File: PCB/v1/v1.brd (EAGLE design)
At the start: 53 x 39 mm, 62 parts, among them U2 AT24C512C-SHD-B

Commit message: quickly added antenna
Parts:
- added U$7: ANTENNA_1LEFT, ant-planar-1:SWRA117D_LEFT
- moved C7 1.68 mm to (32.4, 27.3), turned to 90 degrees
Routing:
- net N$39: track 48.5 -> 40.3 mm
- net N$74: track 0.00 -> 7.95 mm
- net N$43: track 1.63 -> 3.58 mm
- net GND: track 184.4 -> 182.6 mm
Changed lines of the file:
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@@
 <setting verticaltext="up"/>
 </settings>
-<grid distance="0.25" unitdist="mm" unit="mm" style="lines" multiple="1" display="no" altdistance="0.125" altunitdist="mm" altunit="mm"/>
+<grid distance="0.25" unitdist="mm" unit="mm" style="lines" multiple="1" display="no" altdistance="0.01" altunitdist="mm" altunit="mm"/>
 <layers>
 <layer number="1" name="Top" color="4" fill="1" visible="yes" active="yes"/>
@@
 <attribute name="OC_FARNELL" value="-" x="-13.49825" y="-11.42925" size="1.778" layer="27" rot="R270" display="off"/>
 </element>
-<element name="C7" library="AVX_By_element14_Batch_1" package="CAPC1005X60N" value="0.5pF" x="31.27895" y="26.062">
-<attribute name="OC_NEWARK" value="32T8767" x="103.66895" y="-18.388" size="1.778" layer="27" display="off"/>
-<attribute name="TOLERANCE" value="±.1 pF" x="103.66895" y="-18.388" size="1.778" layer="27" display="off"/>
-<attribute name="MPN" value="UQCL2A0R5BAT2A/500" x="103.66895" y="-18.388" size="1.778" layer="27" display="off"/>
-<attribute name="SUPPLIER" value="AVX" x="103.66895" y="-18.388" size="1.778" layer="27" display="off"/>
-<attribute name="VOLTAGERATING" value="200V" x="103.66895" y="-18.388" size="1.778" layer="27" display="off"/>
-<attribute name="OC_FARNELL" value="-" x="103.66895" y="-18.388" size="1.778" layer="27" display="off"/>
+<element name="C7" library="AVX_By_element14_Batch_1" package="CAPC1005X60N" value="0.5pF" x="32.438" y="27.27895" rot="R90">
+<attribute name="OC_NEWARK" value="32T8767" x="76.888" y="99.66895" size="1.778" layer="27" rot="R90" display="off"/>
+<attribute name="TOLERANCE" value="±.1 pF" x="76.888" y="99.66895" size="1.778" layer="27" rot="R90" display="off"/>
+<attribute name="MPN" value="UQCL2A0R5BAT2A/500" x="76.888" y="99.66895" size="1.778" layer="27" rot="R90" display="off"/>
+<attribute name="SUPPLIER" value="AVX" x="76.888" y="99.66895" size="1.778" layer="27" rot="R90" display="off"/>
+<attribute name="VOLTAGERATING" value="200V" x="76.888" y="99.66895" size="1.778" layer="27" rot="R90" display="off"/>
+<attribute name="OC_FARNELL" value="-" x="76.888" y="99.66895" size="1.778" layer="27" rot="R90" display="off"/>
 </element>
 <element name="C9" library="AVX_By_element14_Batch_1" package="CAPC1005X60N" value="33p" x="37.75" y="21.47" rot="R90">
@@
 <attribute name="SPICEPREFIX" value="R" x="4.1717" y="10.40475" size="1.778" layer="28" rot="MR180" display="off"/>
 </element>
+<element name="U$7" library="ant-planar-1" package="SWRA117D_LEFT" value="ANTENNA_1LEFT" x="35.5" y="30.75"/>
 </elements>
 <signals>
@@
 <wire x1="30.5023" y1="27.90495" x2="30.5023" y2="28.7523" width="0.25" layer="1"/>
 <wire x1="30.5023" y1="28.7523" x2="30.9363" y2="29.1863" width="0.25" layer="1"/>
-<wire x1="31.76155" y1="26.062" x2="31.76155" y2="26.26155" width="0.25" layer="1"/>
-<wire x1="31.76155" y1="26.26155" x2="32.25" y2="26.75" width="0.25" layer="1"/>
-<wire x1="32.25" y1="26.75" x2="32.25" y2="28.5" width="0.25" layer="1"/>
-<wire x1="32.25" y1="28.5" x2="32.125" y2="28.625" width="0.25" layer="1"/>
 <wire x1="32.125" y1="28.625" x2="32" y2="28.75" width="0.25" layer="1"/>
 <wire x1="32" y1="28.75" x2="31.3726" y2="28.75" width="0.25" layer="1"/>
@@
 <wire x1="40" y1="25.25" x2="45.25" y2="25.25" width="0.25" layer="1"/>
 <wire x1="45.25" y1="25.25" x2="45.5" y2="25" width="0.25" layer="1"/>
+<wire x1="32.125" y1="28.625" x2="32.438" y2="28.312" width="0.25" layer="1"/>
+<wire x1="32.438" y1="28.312" x2="32.438" y2="27.76155" width="0.25" layer="1"/>
 <wire x1="6" y1="4.25" x2="7.004740625" y2="2.612" width="0" layer="19" extent="1-1"/>
+<wire x1="32.438" y1="27.76155" x2="39.84175" y2="25.09175" width="0" layer="19" extent="1-1"/>
 </signal>
 <signal name="N$28">
@@
 <wire x1="38.69" y1="16.3286" x2="38.4386" y2="16.58" width="0.25" layer="1"/>
 <wire x1="38.7126" y1="15.7274" x2="38.69" y2="15.75" width="0.25" layer="1"/>
-<wire x1="29.25" y1="25.35" x2="33.35" y2="25.35" width="0.25" layer="1"/>
-<wire x1="33.35" y1="25.35" x2="40.75" y2="32.75" width="0.25" layer="1"/>
+<wire x1="29.25" y1="25.35" x2="34.1" y2="25.35" width="0.25" layer="1"/>
 <wire x1="38.4386" y1="16.58" x2="38.4386" y2="16.0614" width="0.25" layer="1"/>
 <wire x1="38.4386" y1="16.0614" x2="38.75" y2="15.75" width="0.25" layer="1"/>
@@
 <wire x1="42.875" y1="19.125" x2="42.875" y2="15.75" width="0.25" layer="1"/>
 <wire x1="46.375" y1="20.75" x2="45.5" y2="20.75" width="0.25" layer="1"/>
-<wire x1="46.375" y1="24.5" x2="46.375" y2="20.75" width="0.25" layer="1"/>
+<wire x1="46.375" y1="25.375" x2="46.375" y2="20.75" width="0.25" layer="1"/>
 <wire x1="40.125" y1="15.75" x2="40.06" y2="15.7274" width="0.25" layer="1"/>
 <wire x1="42.875" y1="19.125" x2="43" y2="19.25" width="0.25" layer="1"/>
 <wire x1="43" y1="19.25" x2="44" y2="19.25" width="0.25" layer="1"/>
 <wire x1="44" y1="19.25" x2="45.5" y2="20.75" width="0.25" layer="1"/>
-<wire x1="40.75" y1="32.75" x2="46.5" y2="32.75" width="0.25" layer="1"/>
-<wire x1="46.5" y1="32.75" x2="47.75" y2="31.5" width="0.25" layer="1"/>
-<wire x1="47.75" y1="31.5" x2="47.75" y2="25.875" width="0.25" layer="1"/>
-<wire x1="47.75" y1="25.875" x2="46.375" y2="24.5" width="0.25" layer="1"/>
+<wire x1="34.1" y1="25.35" x2="38.25" y2="29.5" width="0.25" layer="1"/>
+<wire x1="38.25" y1="29.5" x2="42.25" y2="29.5" width="0.25" layer="1"/>
+<wire x1="42.25" y1="29.5" x2="46.375" y2="25.375" width="0.25" layer="1"/>
 </signal>
 <signal name="N$29">
@@
 <contactref element="C7" pad="1"/>
 <contactref element="U$1" pad="RF"/>
-<wire x1="29.25" y1="25.85" x2="30.58435" y2="25.85" width="0.25" layer="1"/>
-<wire x1="30.58435" y1="25.85" x2="30.79635" y2="26.062" width="0.25" layer="1"/>
+<wire x1="29.25" y1="25.85" x2="31.49165" y2="25.85" width="0.25" layer="1"/>
+<wire x1="31.49165" y1="25.85" x2="32.438" y2="26.79635" width="0.25" layer="1"/>
 </signal>
 <signal name="N$48">
@@
 <via x="10.75" y="18.25" extent="1-16" drill="0.6"/>
 </signal>
+<signal name="N$74">
+<wire x1="38" y1="31" x2="38" y2="30.25" width="0.25" layer="1"/>
+<wire x1="38" y1="30.25" x2="34.5" y2="26.75" width="0.25" layer="1"/>
+<wire x1="34.5" y1="26.75" x2="32.25" y2="26.75" width="0.25" layer="1"/>
+</signal>
+<signal name="N$75">
+<via x="34" y="28.5" extent="1-16" drill="0.5"/>
+</signal>
+<signal name="N$76">
+<via x="43.84" y="25.66" extent="1-16" drill="0.5"/>
+</signal>
+<signal name="N$77">
+<via x="49.2" y="28.45" extent="1-16" drill="0.5"/>
+</signal>
+<signal name="N$78">
+<via x="45.82" y="28.7" extent="1-16" drill="0.5"/>
+</signal>
+<signal name="N$79">
+<via x="29.24" y="31.8" extent="1-16" drill="0.5"/>
+</signal>
+<signal name="N$80">
+<via x="33.32" y="34.14" extent="1-16" drill="0.5"/>
+</signal>
+<signal name="N$81">
+<via x="48.75" y="25.52" extent="1-16" drill="0.5"/>
+</signal>
+<signal name="N$82">
+<via x="48.93" y="22.11" extent="1-16" drill="0.5"/>
+</signal>
 </signals>

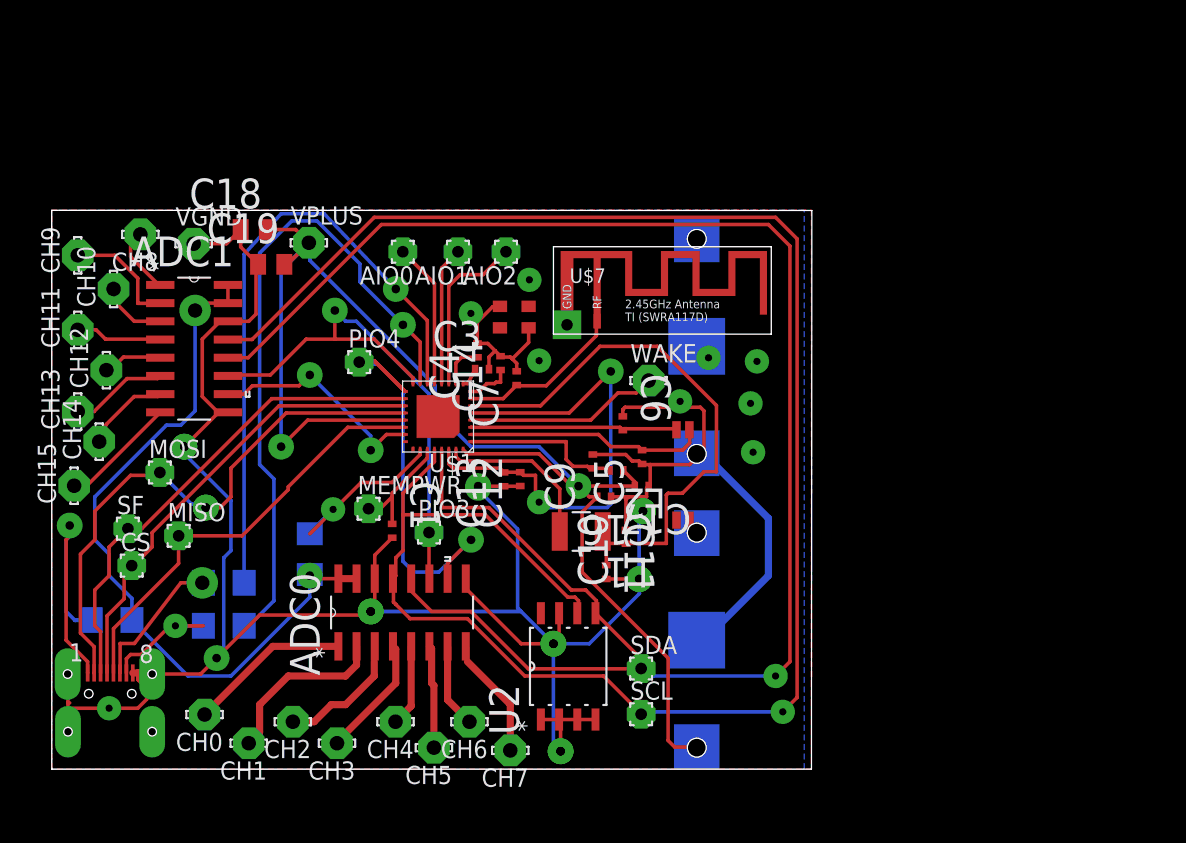
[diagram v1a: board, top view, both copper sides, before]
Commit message: trying to make antenna board edge
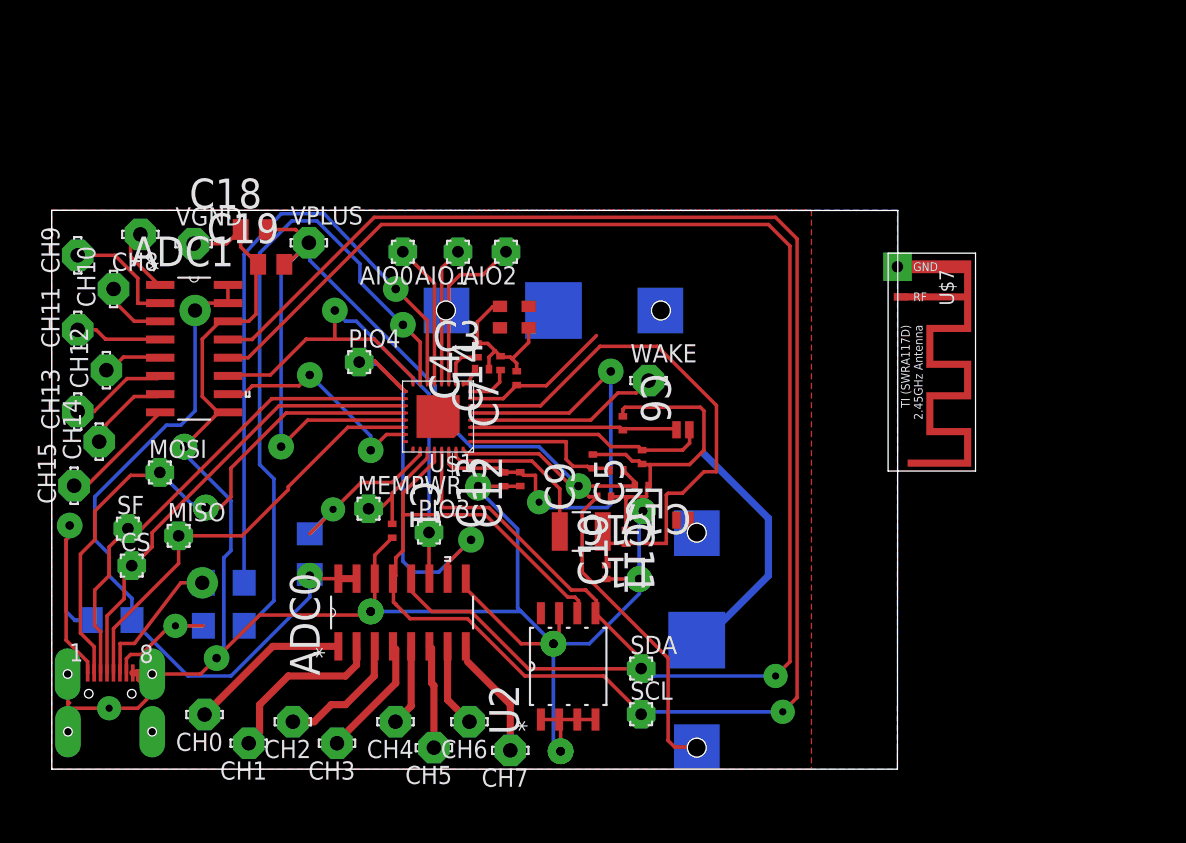
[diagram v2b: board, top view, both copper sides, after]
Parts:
- moved U$7 23.7 mm to (58.8, 35.5), turned to 270 degrees
- moved U$6 10.3 mm to (35.0, 32.0), turned to 0 degrees
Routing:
- net N$74: track 7.95 -> 7.20 mm
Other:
- board size 53 x 39 mm -> 59 x 39 mm
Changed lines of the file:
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@@
 <board>
 <plain>
-<wire x1="0" y1="0" x2="53" y2="0" width="0" layer="20"/>
-<wire x1="53" y1="0" x2="53.0294" y2="38.9786" width="0" layer="20"/>
-<wire x1="53.0294" y1="38.9786" x2="-0.00635" y2="38.98895" width="0" layer="20"/>
+<wire x1="0" y1="0" x2="59" y2="0" width="0" layer="20"/>
+<wire x1="59" y1="0" x2="59.0294" y2="38.9786" width="0" layer="20"/>
+<wire x1="59.0294" y1="38.9786" x2="-0.00635" y2="38.98895" width="0" layer="20"/>
 <wire x1="-0.00635" y1="38.98895" x2="0" y2="0" width="0" layer="20"/>
 </plain>
@@
 <element name="U$4" library="SSP-T7-F" package="SSP-T7-F" value="SSP-T7-F" x="43.2844" y="23.0797" rot="R270"/>
 <element name="U$5" library="BATTERY_2996" package="BATTERY_2996" value="BATTERY_2996" x="45" y="9" rot="MR90"/>
-<element name="U$6" library="BATTERY_2996" package="BATTERY_2996" value="BATTERY_2996" x="45" y="29.5" rot="MR90"/>
+<element name="U$6" library="BATTERY_2996" package="BATTERY_2996" value="BATTERY_2996" x="35" y="32" rot="MR0"/>
 <element name="R5" library="eagle-ltspice" package="R1206" value="" x="18" y="15" rot="MR270">
 <attribute name="SPICEMODEL" value="NONE" x="18" y="15" size="1.778" layer="28" rot="MR270" display="off"/>
@@
 <attribute name="SPICEPREFIX" value="R" x="4.1717" y="10.40475" size="1.778" layer="28" rot="MR180" display="off"/>
 </element>
-<element name="U$7" library="ant-planar-1" package="SWRA117D_LEFT" value="ANTENNA_1LEFT" x="35.5" y="30.75"/>
+<element name="U$7" library="ant-planar-1" package="SWRA117D_LEFT" value="ANTENNA_1LEFT" x="58.75" y="35.5" rot="R270"/>
 </elements>
 <signals>
@@
 <polygon width="0.25" layer="16">
 <vertex x="0" y="0"/>
-<vertex x="52.5" y="0"/>
-<vertex x="52.5" y="39"/>
+<vertex x="59" y="0"/>
+<vertex x="59" y="39"/>
 <vertex x="0" y="39"/>
 </polygon>
@@
 <contactref element="C14" pad="1"/>
 <contactref element="U$1" pad="VDD_XTAL"/>
-<wire x1="29.25" y1="26.35" x2="29.79805" y2="26.35" width="0.25" layer="1"/>
-<wire x1="29.79805" y1="26.35" x2="30.34665" y2="26.8986" width="0.25" layer="1"/>
-<wire x1="30.34665" y1="26.8986" x2="30.8986" y2="26.8986" width="0.25" layer="1"/>
-<wire x1="30.8986" y1="26.8986" x2="31" y2="27" width="0.25" layer="1"/>
-<wire x1="31" y1="27" x2="31.29935" y2="27" width="0.25" layer="1"/>
-<wire x1="31.29935" y1="27" x2="31.31185" y2="26.9875" width="0.25" layer="1"/>
-<wire x1="31.31185" y1="26.9875" x2="31.31185" y2="27.84555" width="0.25" layer="1"/>
-<wire x1="31.31185" y1="27.84555" x2="31.31" y2="27.8474" width="0.25" layer="1"/>
+<wire x1="29.25" y1="26.35" x2="30.6" y2="26.35" width="0.25" layer="1"/>
+<wire x1="30.6" y1="26.35" x2="31.25" y2="27" width="0.25" layer="1"/>
+<wire x1="31.25" y1="27" x2="31.25" y2="27.7874" width="0.25" layer="1"/>
+<wire x1="31.25" y1="27.7874" x2="31.31" y2="27.8474" width="0.25" layer="1"/>
 </signal>
 <signal name="N$19">
@@
 <wire x1="40.6774" y1="19.75" x2="40.6774" y2="20.04425" width="0.25" layer="1"/>
 <wire x1="40.6774" y1="20.04425" x2="39.87405" y2="20.8476" width="0.25" layer="1"/>
+<wire x1="45" y1="1.5375" x2="45" y2="1.5375" width="0" layer="19" extent="1-16"/>
 <wire x1="43.4625" y1="1.5375" x2="45" y2="1.5375" width="0.25" layer="1"/>
 <wire x1="45" y1="1.5375" x2="45" y2="1.5375" width="0" layer="19" extent="1-16"/>
@@
 <wire x1="50" y1="17.5" x2="50" y2="13.5" width="0.5" layer="16"/>
 <wire x1="50" y1="13.5" x2="45.5" y2="9" width="0.5" layer="16"/>
-<wire x1="45.4625" y1="22.0375" x2="45" y2="22.0375" width="0" layer="19" extent="16-16"/>
+<wire x1="45.4625" y1="22.0375" x2="42.4625" y2="32" width="0" layer="19" extent="16-16"/>
 </signal>
 <signal name="N$44">
@@
 </signal>
 <signal name="N$74">
-<wire x1="38" y1="31" x2="38" y2="30.25" width="0.25" layer="1"/>
+<wire x1="38" y1="31" x2="38" y2="30.25" width="0" layer="19" extent="1-16"/>
 <wire x1="38" y1="30.25" x2="34.5" y2="26.75" width="0.25" layer="1"/>
 <wire x1="34.5" y1="26.75" x2="32.25" y2="26.75" width="0.25" layer="1"/>
 </signal>
-<signal name="N$75">
-<via x="34" y="28.5" extent="1-16" drill="0.5"/>
-</signal>
-<signal name="N$76">
-<via x="43.84" y="25.66" extent="1-16" drill="0.5"/>
-</signal>
-<signal name="N$77">
-<via x="49.2" y="28.45" extent="1-16" drill="0.5"/>
-</signal>
-<signal name="N$78">
-<via x="45.82" y="28.7" extent="1-16" drill="0.5"/>
-</signal>
-<signal name="N$79">
-<via x="29.24" y="31.8" extent="1-16" drill="0.5"/>
-</signal>
-<signal name="N$80">
-<via x="33.32" y="34.14" extent="1-16" drill="0.5"/>
-</signal>
-<signal name="N$81">
-<via x="48.75" y="25.52" extent="1-16" drill="0.5"/>
-</signal>
-<signal name="N$82">
-<via x="48.93" y="22.11" extent="1-16" drill="0.5"/>
-</signal>
 </signals>

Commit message: latest
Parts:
- moved U$5 24.9 mm to (35.0, 31.8), turned to 0 degrees
- moved U$6 24.8 mm to (46.0, 9.75), turned to 90 degrees
- moved U$7 10.3 mm to (48.8, 38.0)
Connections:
- net GND: now also U$5.NEG; no longer U$6.NEG
- net N$34: now also U$6.POS@1; no longer U$5.POS@1
- net N$48: now also U$5.POS@1, U$6.NEG; no longer U$5.NEG, U$6.POS@1
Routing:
- net N$21: track 135.9 -> 78.5 mm, vias 1 -> 2
- net N$22: track 126.4 -> 104.2 mm
- net N$76: track 0.00 -> 20.4 mm
- net GND: track 182.6 -> 193.7 mm
- net N$48: track 17.3 -> 24.8 mm
- net N$74: track 7.20 -> 0.00 mm
- net N$34: track 98.7 -> 100.0 mm
- net N$24: track 16.1 -> 17.4 mm
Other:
- board size 59 x 39 mm -> 55 x 39 mm
- board text added: "T Morrison"
- board text added: "V1"

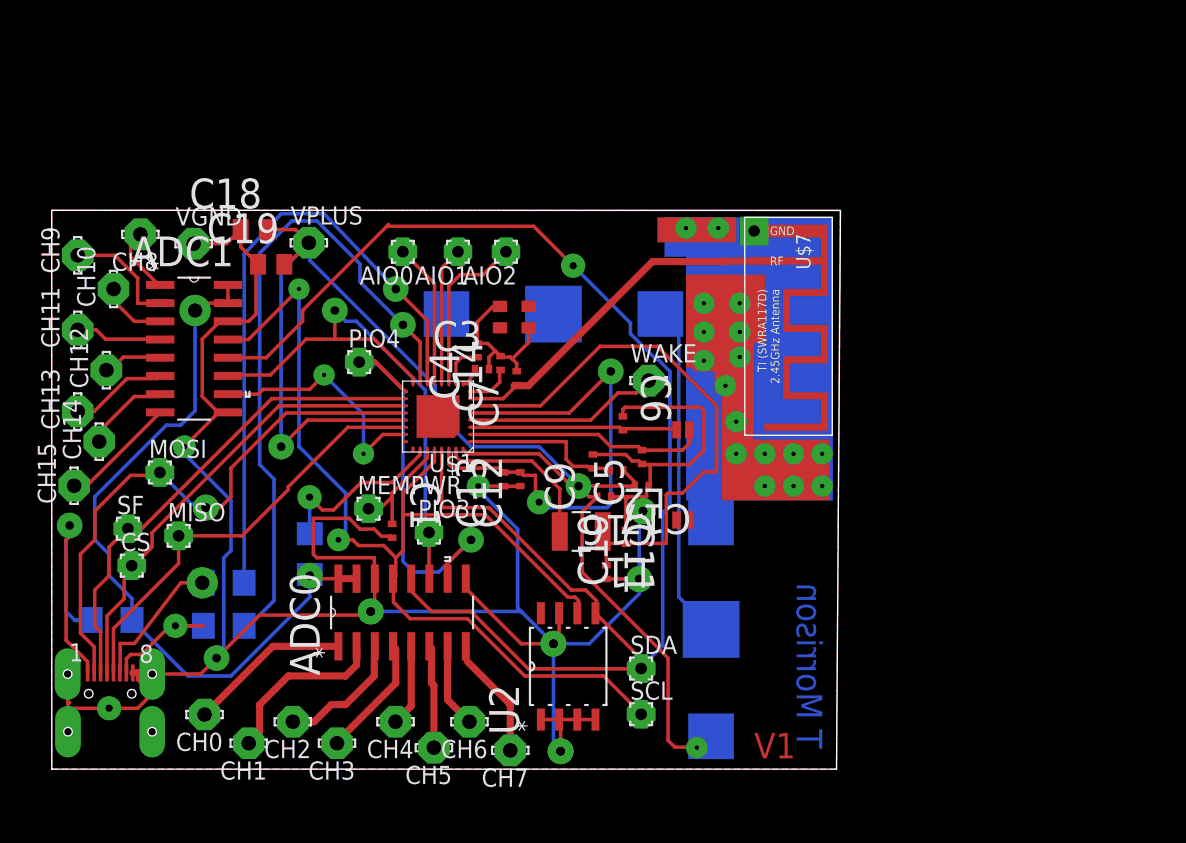
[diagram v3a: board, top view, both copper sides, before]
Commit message: expose pads more and add other ADC
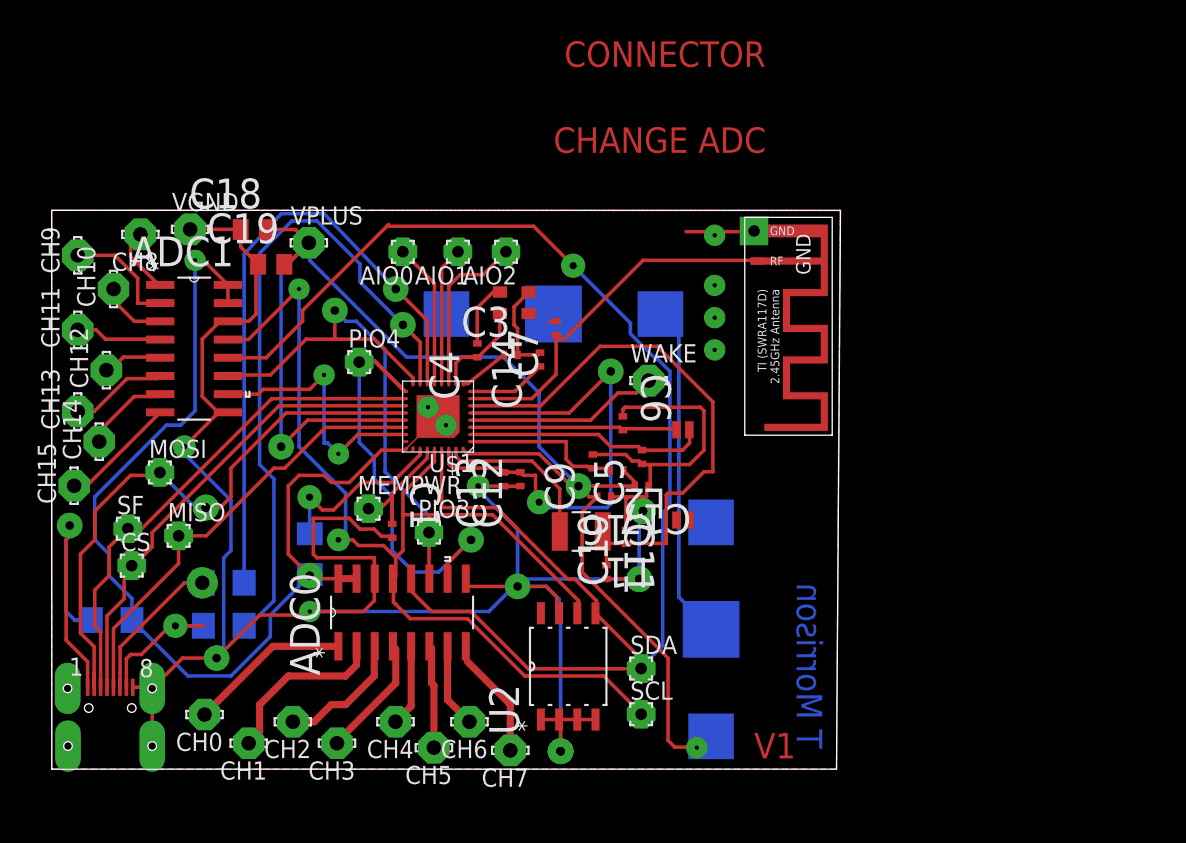
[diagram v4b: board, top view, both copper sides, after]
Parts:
- moved C7 4.45 mm to (35.2, 30.8)
- moved C14 2.76 mm to (34.1, 28.6)
- moved C3 2.24 mm to (32.0, 28.9)
- moved VGND 1.03 mm to (9.65, 37.7)
- moved U$2 1.00 mm to (3.82, 2.88)
- moved U$3 1.00 mm to (32.3, 32.5)
- renumbered U$7 to GND
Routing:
- net VDD: track 51.2 -> 73.1 mm
- net N$76: track 20.4 -> 0.00 mm
- net N$84: track 0.00 -> 16.0 mm, vias 1 -> 0
- net N$43: track 3.58 -> 9.39 mm
- net N$80: track 0.00 -> 4.77 mm, vias 1 -> 0
- net GND: track 193.7 -> 189.5 mm, vias 9 -> 12
- net N$79: track 0.00 -> 3.87 mm, vias 1 -> 0
- net N$35: track 3.14 -> 5.53 mm
- net N$29: track 1.46 -> 3.54 mm
- net N$50: track 39.8 -> 41.8 mm
- net N$34: track 100.0 -> 101.2 mm
- net N$24: track 17.4 -> 18.5 mm
- net N$51: track 34.3 -> 35.3 mm
- net N$36: track 9.27 -> 10.3 mm
- net N$31: track 32.5 -> 33.5 mm
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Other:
- board text added: "CHANGE ADC"
- board text added: "CONNECTOR"
